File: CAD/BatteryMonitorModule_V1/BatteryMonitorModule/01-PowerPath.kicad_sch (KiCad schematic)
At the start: 21 parts, among them J1 OSTYK42105030, K1 G5LE-1, Q1 AO3401A, Q2 IRFZ44NPBF, Q3 MMBT2222A, Q4 MMBT2222A

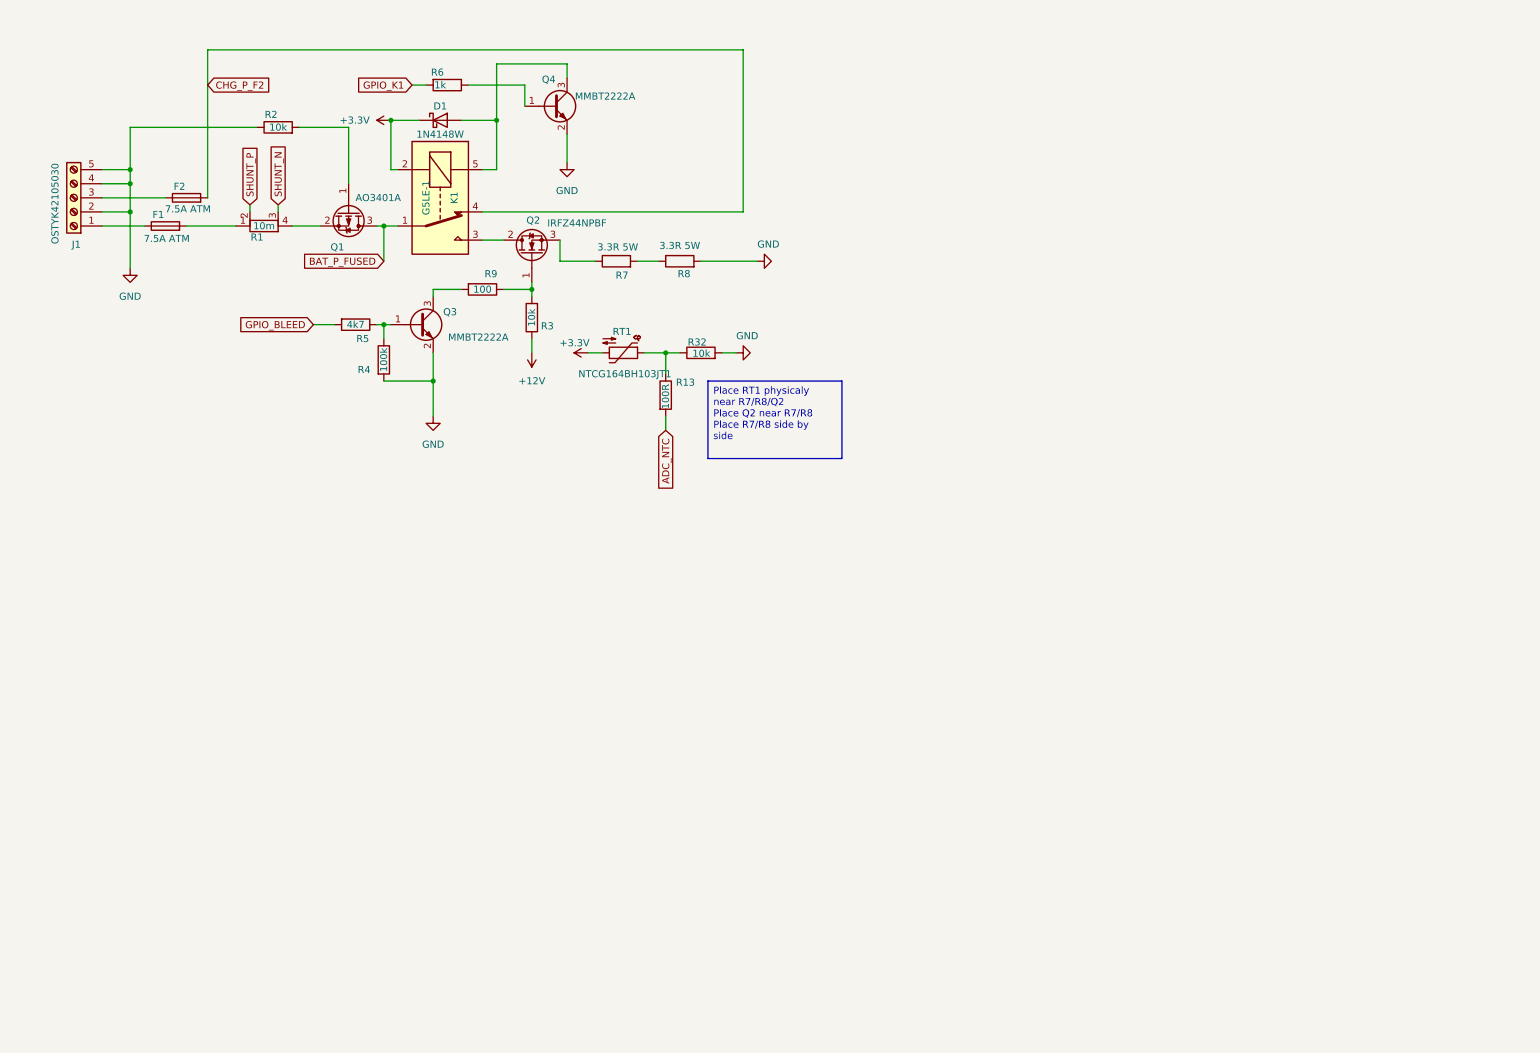
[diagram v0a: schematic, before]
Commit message: V1 schematic rework — PowerPath, PowerSupply, IO updates and custom library additions
Add custom symbols/footprints for Keystone 4966 and AO4407A, and SOIC127P600X175-8N
footprint. Update sym-lib-table to reference new custom library.

Co-Authored-By: Claude Opus 4.7 (1M context) <noreply@anthropic.com>
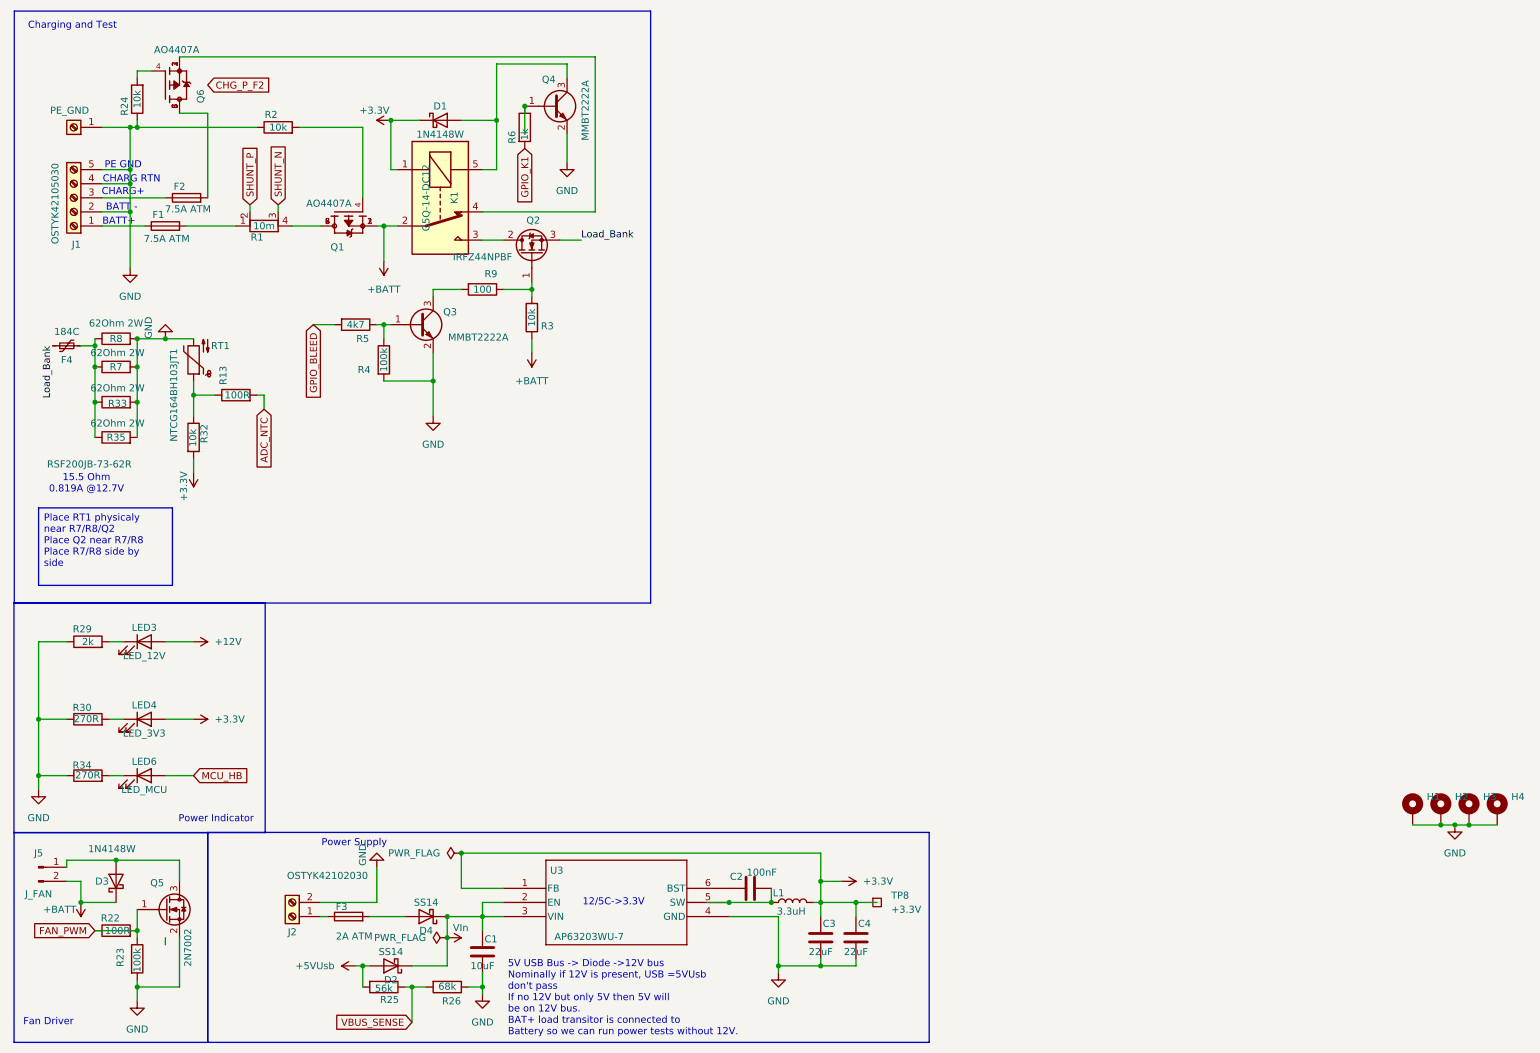
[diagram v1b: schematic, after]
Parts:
- added C1: 10uF, Capacitor_SMD:C_0805_2012Metric, symbol Device:C
- added C2: 100nF, Capacitor_SMD:C_0603_1608Metric, symbol Device:C
- added C3, C4: 22uF, Capacitor_SMD:C_0805_2012Metric, symbol Device:C
- added D2, D4: SS14, Diode_SMD:D_SOD-123, symbol Device:D_Schottky
- added D3: 1N4148W, Diode_SMD:D_SOD-123, symbol Device:D_Schottky
- added F3: 2A ATM, BatteryMonitorModule_Custom:FUSE_BK-6013, symbol Device:Fuse
- added F4: 184C, Resistor_THT:R_Axial_DIN0516_L15.5mm_D5.0mm_P20.32mm_Horizontal, symbol Device:Polyfuse_Small
- added H1, H2, H3, H4: MountingHole_Pad, symbol Mechanical:MountingHole_Pad
- added J2: OSTYK42102030, BatteryMonitorModule_Custom:OSTYK42102030, symbol Connector:Screw_Terminal_01x02
- added J5: J_FAN, Connector_PinHeader_2.54mm:PinHeader_1x02_P2.54mm_Vertical, symbol Connector:Conn_01x02_Pin
- added L1: 3.3uH, BatteryMonitorModule_Custom:IND_BOURNS_SRR4028, symbol Device:L
- added LED3: LED_12V, LED_SMD:LED_0603_1608Metric, symbol Device:LED
- added LED4: LED_3V3, LED_SMD:LED_0603_1608Metric, symbol Device:LED
- added LED6: LED_MCU, LED_SMD:LED_0603_1608Metric, symbol Device:LED
- added PE_GND: Keystone 4966, BatteryMonitorModule_Custom:KEYSTONE_4966, symbol Connector:Screw_Terminal_01x01
- added Q5: 2N7002, Package_TO_SOT_SMD:SOT-23, symbol Transistor_FET:BSS138
- added Q6: AO4407A, AO4407A:SOIC127P600X175-8N, symbol AO4407A:AO4407A
- added R22: 100R, Resistor_SMD:R_0603_1608Metric, symbol Device:R
- added R23: 100k, Resistor_SMD:R_0603_1608Metric, symbol Device:R
- added R24: 10k, Resistor_SMD:R_0603_1608Metric, symbol Device:R
- added R25: 56k, Resistor_SMD:R_0603_1608Metric, symbol Device:R
- added R26: 68k, Resistor_SMD:R_0603_1608Metric, symbol Device:R
- added R29: 2k, Resistor_SMD:R_0603_1608Metric, symbol Device:R
- added R30, R34: 270R, Resistor_SMD:R_0603_1608Metric, symbol Device:R
- added R33, R35: 62Ohm 2W, Resistor_THT:R_Axial_DIN0516_L15.5mm_D5.0mm_P5.08mm_Vertical, symbol Device:R
- added TP8: +3.3V, TestPoint:TestPoint_Pad_2.0x2.0mm, symbol Connector:TestPoint_Square
- added U3: AP63203WU-7, Package_TO_SOT_SMD:SOT-23-6_Handsoldering, symbol AP63205WU-7:AP63205WU-7
- K1: value G5LE-1 -> G5Q-14-DC12; footprint Relay_THT:Relay_SPDT_Omron-G5LE-1 -> Relay_THT:Relay_SPDT_Omron-G5Q-1; symbol Relay:G5LE-1 -> Relay:G5Q-1
- Q1: value AO3401A -> AO4407A; footprint Package_TO_SOT_SMD:SOT-23 -> AO4407A:SOIC127P600X175-8N; symbol Transistor_FET:AO3401A -> AO4407A:AO4407A; MANUFACTURER (none) -> Alpha & Omega Semiconductor; MAXIMUM_PACKAGE_HEIGHT (none) -> 1.75 mm; PARTREV (none) -> I; STANDARD (none) -> IPC 7351B
- R7, R8: value 3.3R 5W -> 62Ohm 2W; footprint BatteryMonitorModule_Custom:YAG_SQP500_YAG -> Resistor_THT:R_Axial_DIN0516_L15.5mm_D5.0mm_P5.08mm_Vertical
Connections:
- net +12V: now also LED3.2 (A); no longer R3.1
- net +3.3V: now also K1.1, R32.2, C3.1, C4.1, L1.2, LED4.2 (A), TP8.1, U3.1 (FB); no longer K1.2, RT1.2
- net CHG_P_F2: no longer F2.2, K1.4
- net GND: now also R7.2, RT1.2, C1.2, C3.2, C4.2, H1.1, H2.1, H3.1, H4.1, J2.2 (Pin_2), PE_GND.1 (Pin_1), Q5.2 (S), R23.2, R24.1, R26.1, R29.1, R30.1, R33.2, R34.1, R35.2, U3.4 (GND); no longer R32.2
- net at R1.4: now also Q1.5, Q1.6, Q1.7, Q1.8; no longer Q1.2 (S)
- net at R8.1: now also R7.1, F4.2, R33.1, R35.1; no longer R7.2
- net Load_Bank: now reaches Q2.3 (S)
- net Load_Bank: now also F4.1; no longer R7.1
- net at R2.2: now also Q1.4; no longer Q1.1 (G)
- net BAT_P_FUSED renamed +BATT
- net +BATT: now also K1.2, Q1.1, Q1.2, R3.1, D3.1 (K), J5.2 (Pin_2); no longer K1.1
- new net: C2.2, L1.1, U3.5 (SW)
- new net: D3.2 (A), J5.1 (Pin_1), Q5.3 (D)
- new net: LED3.1 (K), R29.2
- new net: K1.4, Q6.1, Q6.2, Q6.3
- new net: F3.1, J2.1 (Pin_1)
- new net: C2.1, U3.6 (BST)
- new net: LED6.1 (K), R34.2
- new net: Q6.4, R24.2
- new net: F2.2, Q6.5, Q6.6, Q6.7, Q6.8
- new net: D4.2 (A), F3.2
- new net: LED4.1 (K), R30.2
- new net +5VUsb: D2.2 (A), R25.2
- new net FAN_PWM: Q5.1 (G), R22.1, R22.2, R23.1
- new net MCU_HB: LED6.2 (A)
- new net VBUS_SENSE: R25.1, R26.2
- new net VIn: C1.1, D2.1 (K), D4.1 (K), U3.2 (EN), U3.3 (VIN)
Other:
- note added: "12/5C->3.3V"
- note added: "15.5 Ohm 0.819A @12.7V"
- note added: "5V USB Bus -> Diode ->12V bus Nominally if 12V is present, USB =5VUsb don't pass If no 12V but only 5V then 5V will be on 12V bus. BAT+ load transitor is connected to Battery so we can run power tests without 12V."
- note added: "BATT -"
- note added: "BATT+"
- note added: "CHARG RTN"
- note added: "CHARG+"
- note added: "Charging and Test"
- note added: "Fan Driver"
- note added: "PE GND"
- note added: "Power Indicator"
- note added: "Power Supply"
- moved on the sheet: R13, R32, R6, R7, R8, RT1

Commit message: add QT06ADP83H0000G and UJ20-C USB-C connector symbols/footprints/3D models
Update V1 schematics (PowerPath, MCU, IO, top-level) to incorporate new parts.

Co-Authored-By: Claude Opus 4.7 (1M context) <noreply@anthropic.com>
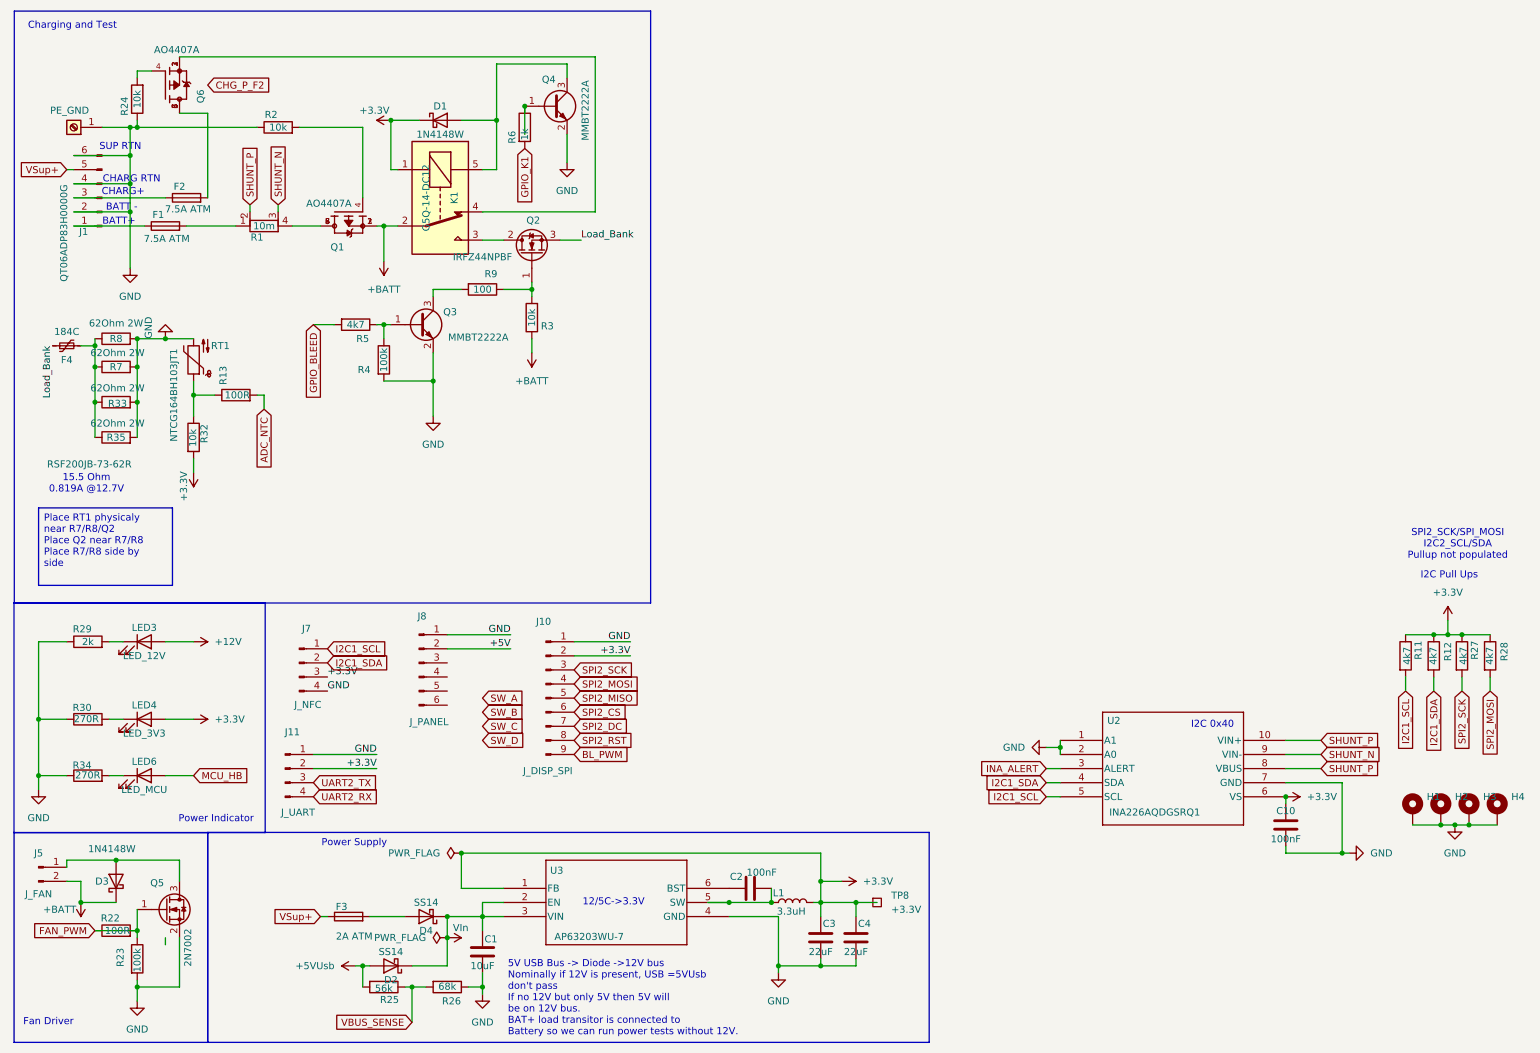
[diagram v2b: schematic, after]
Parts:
- removed J2: OSTYK42102030, BatteryMonitorModule_Custom:OSTYK42102030, symbol Connector:Screw_Terminal_01x02
- added C10: 100nF, Capacitor_SMD:C_0603_1608Metric, symbol Device:C
- added J10: J_DISP_SPI, Connector_JST:JST_XH_B9B-XH-A_1x09_P2.50mm_Vertical, symbol Connector:Conn_01x09_Pin
- added J11: J_UART, Connector_PinHeader_2.54mm:PinHeader_1x04_P2.54mm_Vertical, symbol Connector:Conn_01x04_Pin
- added J7: J_NFC, Connector_JST:JST_XH_B4B-XH-A_1x04_P2.50mm_Vertical, symbol Connector:Conn_01x04_Pin
- added J8: J_PANEL, Connector_JST:JST_XH_B6B-XH-A_1x06_P2.50mm_Vertical, symbol Connector:Conn_01x06_Pin
- added R11, R12, R27, R28: 4k7, Resistor_SMD:R_0603_1608Metric, symbol Device:R
- added U2: INA226AQDGSRQ1, Package_SO:MSOP-10_3x3mm_P0.5mm, symbol INA226AQDGSRQ1:INA226AQDGSRQ1
- J1: value OSTYK42105030 -> QT06ADP83H0000G; footprint BatteryMonitorModule_Custom:OSTYK42105030 -> BatteryMonitorModule_Custom:QT06ADP83H0000G; symbol Connector:Screw_Terminal_01x05 -> Connector:Conn_01x06_Pin
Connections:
- net +3.3V: now also C10.1, J10.2 (Pin_2), J11.2 (Pin_2), J7.3 (Pin_3), R11.1, R12.1, R27.1, R28.1, U2.6 (VS)
- net GND: now also J1.6 (Pin_6), C10.2, J10.1 (Pin_1), J11.1 (Pin_1), J7.4 (Pin_4), J8.1 (Pin_1), U2.1 (A1), U2.2 (A0), U2.7 (GND); no longer J1.5 (Pin_5)
- net SHUNT_N: now also U2.9 (VIN-)
- net SHUNT_P: now also U2.10 (VIN+), U2.8 (VBUS)
- net VSup+: now reaches F3.1
- net VSup+: now also J1.5 (Pin_5)
- new net +5V: J8.2 (Pin_2)
- new net BL_PWM: J10.9 (Pin_9)
- new net I2C1_SCL: J7.1 (Pin_1), R11.2, U2.5 (SCL)
- new net I2C1_SDA: J7.2 (Pin_2), R12.2, U2.4 (SDA)
- new net INA_ALERT: U2.3 (ALERT)
- new net SPI2_CS: J10.6 (Pin_6)
- new net SPI2_DC: J10.7 (Pin_7)
- new net SPI2_MISO: J10.5 (Pin_5)
- new net SPI2_MOSI: J10.4 (Pin_4), R28.2
- new net SPI2_RST: J10.8 (Pin_8)
- new net SPI2_SCK: J10.3 (Pin_3), R27.2
- new net UART2_RX: J11.4 (Pin_4)
- new net UART2_TX: J11.3 (Pin_3)
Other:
- note added: "I2C 0x40"
- note added: "I2C Pull Ups"
- note added: "SPI2_SCK/SPI_MOSI I2C2_SCL/SDA Pullup not populated"
- note added: "SUP RTN"
- note removed: "PE GND"
